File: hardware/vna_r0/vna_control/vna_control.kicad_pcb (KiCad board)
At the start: 2 copper layers, 111 parts, among them J301 CONN_02X10, J302 CONN_02X10, J303 CONN_02X10, J304 CONN_02X23, J305 CONN_01X02, J306 CONN_02X23, J307 BARREL_JACK, J401 CONN_01X02, Q301 DMG2305UX, U201 AD9577, U202 CONN_SMA_2GND, U301 CONN_SMA, U302 CONN_SMA, U303 CONN_SMA, U304 CONN_SMA, U305 CONN_SMA, U401 ADP7158, U402 ADP7158, U403 ADP7158, U404 OKR-T/3-W12-C, U405 TPS2041B, U406 LTC1983, Y201 26 MHz FX532A

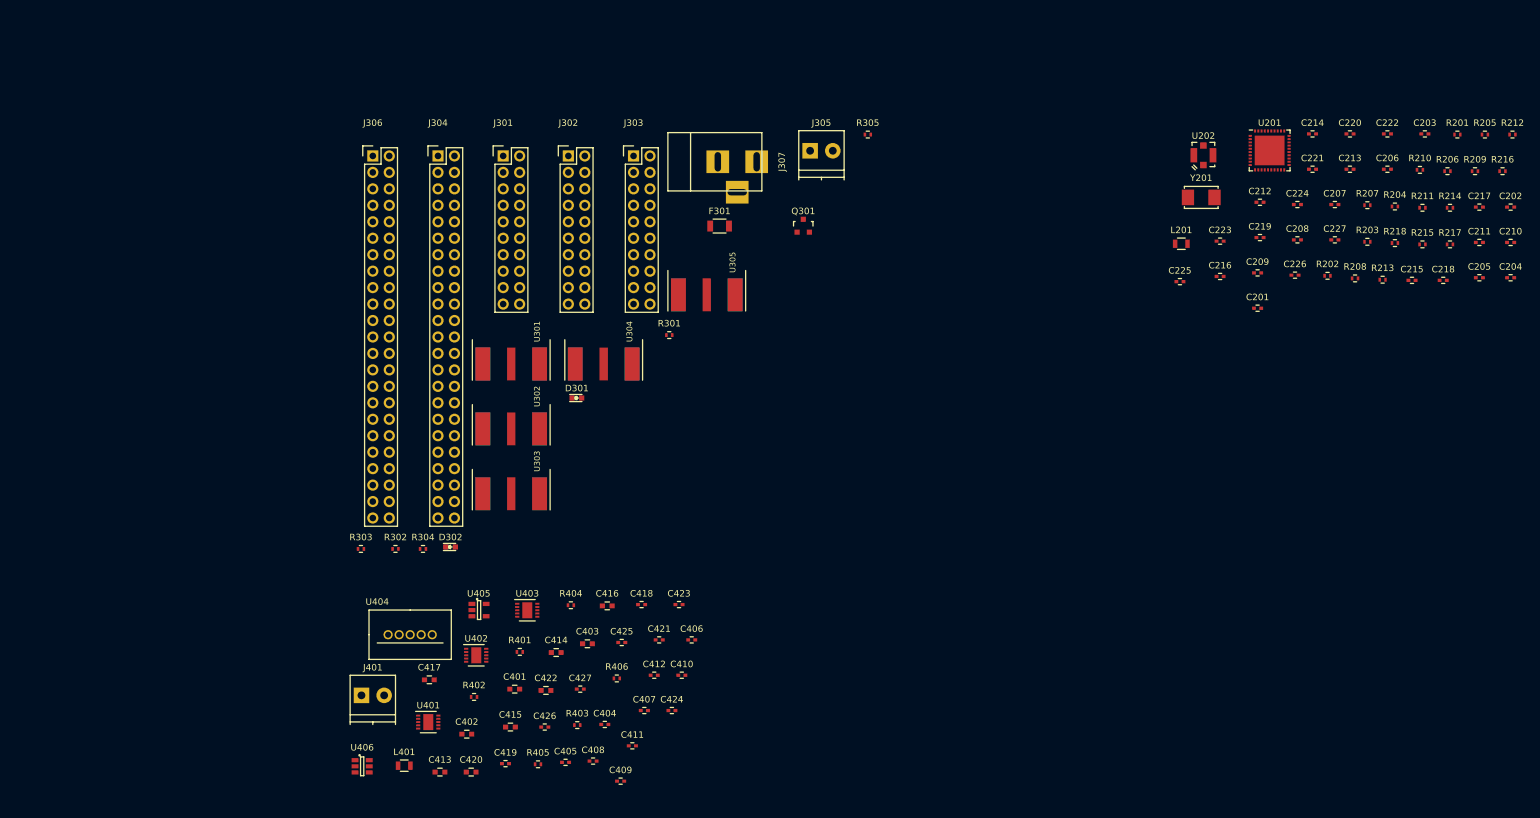
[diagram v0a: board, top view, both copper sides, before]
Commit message: component placement on vna cape..
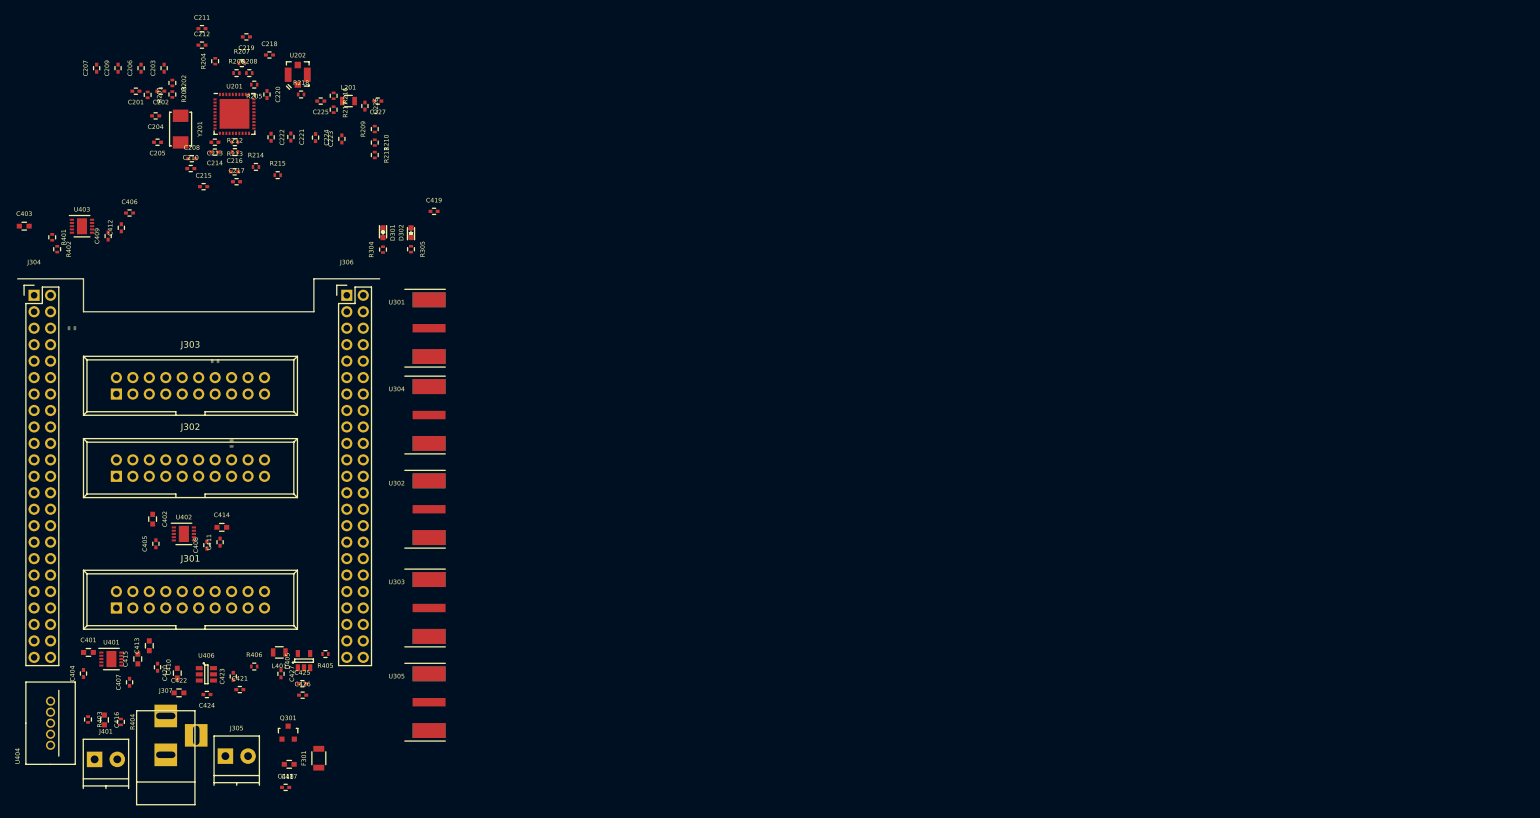
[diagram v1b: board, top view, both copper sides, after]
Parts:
- J301, J302, J303: footprint Pin_Headers:Pin_Header_Straight_2x10 -> Connect:IDC_Header_Straight_20pins
- R301, R302, R303: moved to B.Cu
- moved C204 210.6 mm to (54.3, 40.9), turned to 180 degrees
- moved C202 209.1 mm to (55.1, 37.1), turned to 180 degrees
- moved C205 205.1 mm to (54.6, 45.0), turned to 180 degrees
- moved C210 204.0 mm to (59.7, 49.0)
- moved R201 202.2 mm to (53.1, 37.6), turned to 270 degrees
- moved C211 199.9 mm to (61.5, 27.4)
- moved R212 197.2 mm to (66.5, 46.5)
- moved C203 194.8 mm to (55.6, 33.5), turned to 90 degrees
- moved C206 193.0 mm to (52.1, 33.5), turned to 90 degrees
- moved C207 192.3 mm to (45.2, 33.5), turned to 90 degrees
- moved C217 191.9 mm to (66.8, 51.1)
- moved R205 190.1 mm to (69.5, 36.1), turned to 180 degrees
- moved R206 187.5 mm to (66.8, 34.3)
- moved C215 187.1 mm to (61.7, 51.8)
- moved R203 185.8 mm to (56.9, 37.6), turned to 270 degrees
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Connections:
- D301 pad 1: (no net) -> GND
- D302 pad 2: (no net) -> GND
- R304 pad 1: /connecors/3V3_RF -> +3V3
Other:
- board outline added: 55.9 x 5.1 mm
- copper layers 2 -> 4
- rule pad_to_mask_clearance: 0.2 -> 0.05

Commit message: layout of control cape..
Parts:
- removed C417: CP_Small, Capacitors_SMD:C_0603
- removed C419: 100 nF, Capacitors_SMD:C_0402
- added C428: 100 uF, Capacitors_SMD:c_elec_10x10, F.Cu at (73.2, 123.3)
- R402: moved to B.Cu
- R404: footprint Resistors_SMD:R_0402 -> Resistors_SMD:R_1206
- moved D302 73.6 mm to (43.9, 113.2)
- moved R305 73.6 mm to (43.9, 115.6), turned to 90 degrees
- moved C211 51.4 mm to (64.8, 78.7), turned to 180 degrees
- moved C227 49.8 mm to (80.3, 87.7), turned to 90 degrees
- moved C212 47.6 mm to (64.8, 77.5), turned to 180 degrees
- moved C219 47.2 mm to (68.8, 75.9)
- moved C207 46.9 mm to (59.2, 78.3)
- moved R209 46.8 mm to (77.0, 88.4)
- moved C226 46.7 mm to (79.8, 85.6), turned to 180 degrees
- moved C209 46.3 mm to (60.5, 78.2)
- moved C218 45.8 mm to (68.8, 77.2), turned to 180 degrees
- moved C206 45.7 mm to (61.7, 78.2)
- moved C203 45.3 mm to (63.0, 78.2)
- moved C201 45.0 mm to (52.8, 82.0), turned to 270 degrees
- moved L201 44.8 mm to (80.3, 83.2), turned to 270 degrees
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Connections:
- C427 pad 1: +5V -> Net-(C427-Pad1)
- J401 pad 1: GND -> VPP
- J401 pad 2: VPP -> GND
- L401 pad 1: Net-(L401-Pad1) -> Net-(C427-Pad1)
- U405 pad 5: Net-(L401-Pad1) -> Net-(C427-Pad1)
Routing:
- net +3V3: track 0.00 -> 74.3 mm, vias 0 -> 18
- net GND: track 0.00 -> 66.5 mm, vias 0 -> 80
- net +5V: track 0.00 -> 44.6 mm, vias 0 -> 2
- net VPP: track 0.00 -> 33.3 mm
- net Net-(F301-Pad2): track 0.00 -> 15.9 mm
- net /3V3_PLL_EN: track 0.00 -> 11.7 mm, vias 0 -> 2
- net /clock_gen/OUT1N: track 0.00 -> 11.1 mm
- net Net-(C205-Pad1): track 0.00 -> 10.6 mm
- net Net-(C204-Pad1): track 0.00 -> 10.0 mm
- net Net-(C202-Pad1): track 0.00 -> 9.99 mm
- net /clock_gen/OUT0P: track 0.00 -> 8.78 mm
- net /clock_gen/OUT0N: track 0.00 -> 8.54 mm
- net /clock_gen/OUT3P: track 0.00 -> 8.45 mm
- net /clock_gen/SYNTH_REF_B: track 0.00 -> 7.71 mm
- net Net-(R404-Pad2): track 0.00 -> 7.68 mm
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- added copper zone on F.Cu, net GND
- added copper zone on In1.Cu, net GND
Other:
- board size 55.9 x 5.1 mm -> 73.7 x 76.2 mm
- net class Default: clearance 0.2 -> 0.126
- rule trace_clearance: 0.2 -> 0.126
- board text added: "3V6"
- board text added: "5V IN"
- board text added: "demod"
- board text added: "rf"
- board text added: "vna control cape r1 2017.07"

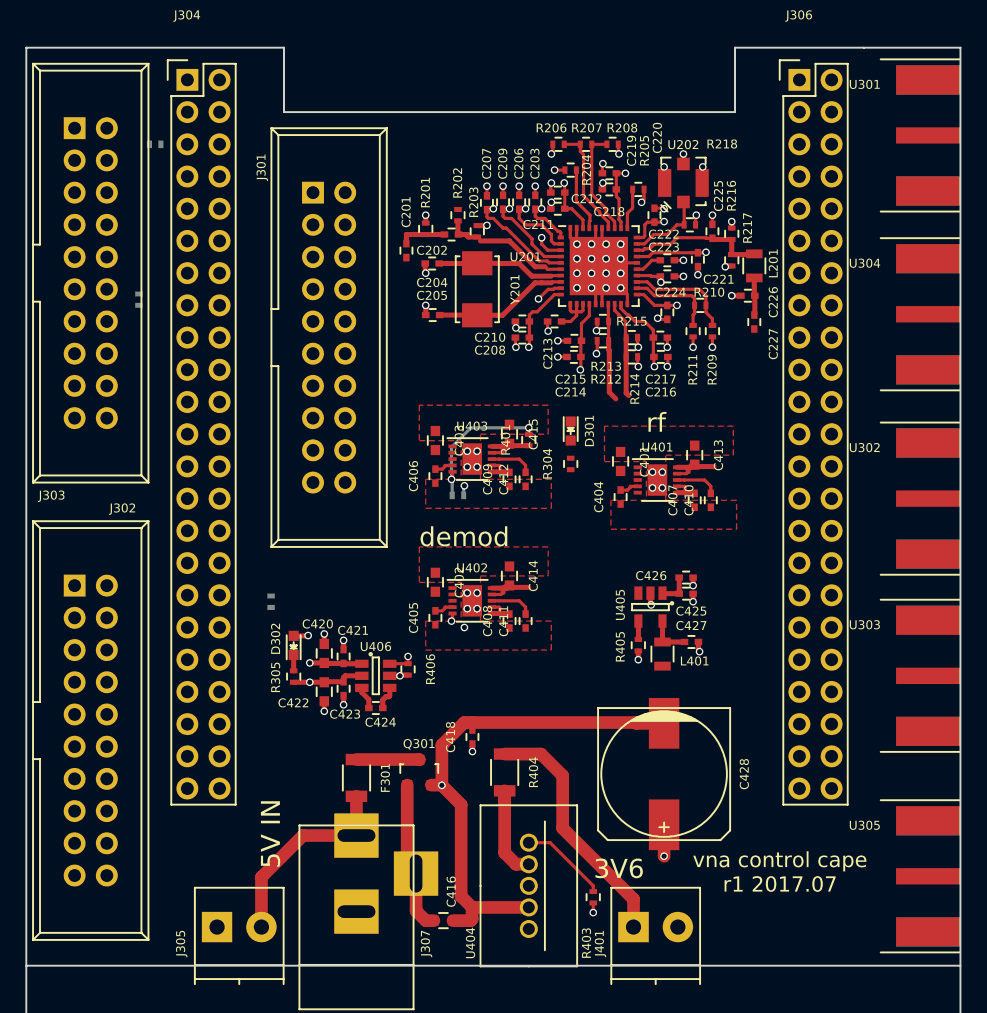
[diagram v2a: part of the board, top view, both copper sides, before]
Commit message: vna control cape layout - all nets connected
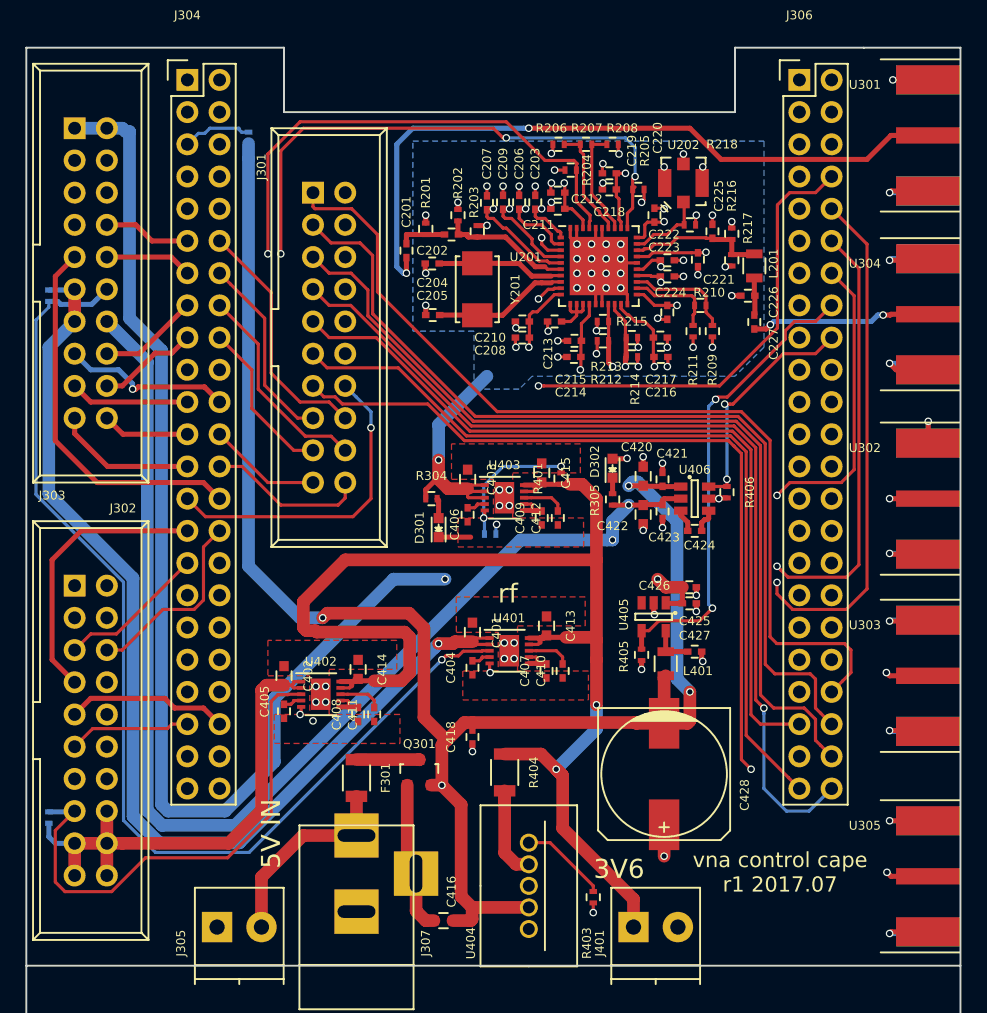
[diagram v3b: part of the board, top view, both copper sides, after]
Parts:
- moved C421 28.8 mm to (73.0, 100.1)
- moved C420 28.8 mm to (71.5, 99.8)
- moved C422 28.8 mm to (71.5, 102.9)
- moved C423 28.8 mm to (73.0, 102.6)
- moved C424 28.8 mm to (75.6, 104.1)
- moved R406 28.8 mm to (78.1, 101.1)
- moved U406 28.8 mm to (75.6, 101.6)
- moved D302 28.8 mm to (69.1, 99.2)
- moved R305 28.8 mm to (69.1, 101.7)
- moved R301 24.4 mm to (24.6, 126.7)
- moved C401 17.8 mm to (58.0, 112.1)
- moved C404 17.8 mm to (58.0, 114.9)
- moved C407 17.8 mm to (63.9, 115.2)
- moved C410 17.8 mm to (65.2, 115.2)
- moved C413 17.8 mm to (63.9, 111.6)
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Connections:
- J304 pad 13: /connecors/DEMOD_LMX_MUXOUT -> /connecors/RF_LMX_CE
- J304 pad 15: (no net) -> /connecors/RF_PORT_SEL
- J304 pad 16: /connecors/AD_PE_B -> /connecors/AD_PE_A
- J304 pad 18: /connecors/AD_PE_A -> /connecors/AD_PE_C
- J304 pad 23: /connecors/RF_SW_1 -> /connecors/RF_SW_2
- J304 pad 25: /connecors/RF_SW_2 -> /connecors/RF_SW_1
- J304 pad 26: /connecors/AD_PE_C -> /connecors/AD_PE_B
- J304 pad 27: /connecors/RF_PORT_SEL -> /connecors/AD_DOUTB
- J304 pad 30: (no net) -> /connecors/DEMOD_LMX_MUXOUT
- J304 pad 41: (no net) -> /connecors/DEMOD_LMX_CE
- J306 pad 10: /3V3_PLL_EN -> /3V3_RF_EN
- J306 pad 11: /connecors/RF_LMX_CE -> (no net)
- J306 pad 12: /3V3_RF_EN -> /3V3_DEMOD_EN
- J306 pad 13: /connecors/DEMOD_LMX_CE -> (no net)
- J306 pad 14: /3V3_DEMOD_EN -> /3V3_PLL_EN
- J306 pad 15: /connecors/MIX_EN -> (no net)
- J306 pad 17: /connecors/MIX_X2 -> (no net)
- J306 pad 26: /connecors/AD_DOUTB -> (no net)
- J306 pad 27: (no net) -> /connecors/MIX_X2
- J306 pad 28: (no net) -> /connecors/MIX_EN
- J306 pad 29: (no net) -> /connecors/IF_REF_EN
- J306 pad 30: (no net) -> /connecors/ADC_CLK_EN
- J306 pad 7: /connecors/IF_REF_EN -> (no net)
- J306 pad 9: /connecors/ADC_CLK_EN -> (no net)
- U302 pad 1: /clock_gen/SYNTH_REF_B -> /clock_gen/SYNTH_REF_A
- U303 pad 1: /clock_gen/SYNTH_REF_A -> /clock_gen/SYNTH_REF_B
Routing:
- net /connecors/AMP_5V: track 2.60 -> 113.5 mm, vias 0 -> 2
- net -5V: track 5.79 -> 95.4 mm, vias 1 -> 2
- net +5V: track 44.6 -> 131.8 mm, vias 2 -> 4
- net /connecors/3V3_RF_SENSE: track 0.00 -> 85.9 mm, vias 0 -> 1
- net /connecors/3V3_RF: track 0.00 -> 84.3 mm, vias 0 -> 1
- net /clock_gen/ADC_CLK: track 2.21 -> 84.8 mm, vias 1 -> 2
- net /3V3_DEMOD_EN: track 0.71 -> 82.1 mm, vias 1 -> 2
- net /connecors/AD_DOUTA_A: track 0.00 -> 74.0 mm, vias 0 -> 1
- net /connecors/AD_DOUTA_D: track 0.00 -> 73.7 mm
- net /connecors/AD_DOUTA_C: track 0.00 -> 71.4 mm
- net /connecors/AD_DOUTA_B: track 0.00 -> 70.9 mm
- net VPP: track 33.3 -> 103.7 mm, vias 0 -> 2
- net /3V3_RF_EN: track 0.00 -> 66.6 mm, vias 0 -> 2
- net /connecors/AD_CLKOUT: track 0.00 -> 65.7 mm
- net /connecors/AD_FS: track 0.00 -> 65.4 mm, vias 0 -> 1
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- added copper zone on B.Cu, net +3V3
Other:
- board text removed: "demod"

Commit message: finished vna control cape
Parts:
- added G***: LOGO, vna_footprints:snail, B.Cu at (83.3, 134.1)
- added REF**: VIA_OSH4LAYER_MIN, vna_footprints:VIA_OSH4LAYER_MIN, F.Cu at (56.5, 99.1)
- added REF**: VIA_OSH4LAYER_MIN, vna_footprints:VIA_OSH4LAYER_MIN, F.Cu at (52.7, 99.1)
- added REF**: VIA_OSH4LAYER_MIN, vna_footprints:VIA_OSH4LAYER_MIN, F.Cu at (52.7, 101.0)
- added REF**: VIA_OSH4LAYER_MIN, vna_footprints:VIA_OSH4LAYER_MIN, F.Cu at (52.7, 102.9)
- added REF**: VIA_OSH4LAYER_MIN, vna_footprints:VIA_OSH4LAYER_MIN, F.Cu at (52.7, 104.8)
- added REF**: VIA_OSH4LAYER_MIN, vna_footprints:VIA_OSH4LAYER_MIN, F.Cu at (56.5, 102.2)
- added REF**: VIA_OSH4LAYER_MIN, vna_footprints:VIA_OSH4LAYER_MIN, F.Cu at (56.5, 103.5)
- added REF**: VIA_OSH4LAYER_MIN, vna_footprints:VIA_OSH4LAYER_MIN, F.Cu at (61.0, 104.1)
- added REF**: VIA_OSH4LAYER_MIN, vna_footprints:VIA_OSH4LAYER_MIN, F.Cu at (62.2, 103.5)
- added REF**: VIA_OSH4LAYER_MIN, vna_footprints:VIA_OSH4LAYER_MIN, F.Cu at (66.0, 103.5)
- added REF**: VIA_OSH4LAYER_MIN, vna_footprints:VIA_OSH4LAYER_MIN, F.Cu at (66.0, 116.2)
- added REF**: VIA_OSH4LAYER_MIN, vna_footprints:VIA_OSH4LAYER_MIN, F.Cu at (58.4, 99.1)
- added REF**: VIA_OSH4LAYER_MIN, vna_footprints:VIA_OSH4LAYER_MIN, F.Cu at (66.0, 117.5)
- added REF**: VIA_OSH4LAYER_MIN, vna_footprints:VIA_OSH4LAYER_MIN, F.Cu at (65.4, 116.8)
- added REF**: VIA_OSH4LAYER_MIN, vna_footprints:VIA_OSH4LAYER_MIN, F.Cu at (64.1, 116.8)
- added REF**: VIA_OSH4LAYER_MIN, vna_footprints:VIA_OSH4LAYER_MIN, F.Cu at (63.5, 117.5)
- added REF**: VIA_OSH4LAYER_MIN, vna_footprints:VIA_OSH4LAYER_MIN, F.Cu at (61.6, 116.2)
- added REF**: VIA_OSH4LAYER_MIN, vna_footprints:VIA_OSH4LAYER_MIN, F.Cu at (61.6, 117.5)
- added REF**: VIA_OSH4LAYER_MIN, vna_footprints:VIA_OSH4LAYER_MIN, F.Cu at (59.7, 117.5)
- added REF**: VIA_OSH4LAYER_MIN, vna_footprints:VIA_OSH4LAYER_MIN, F.Cu at (59.7, 116.2)
- added REF**: VIA_OSH4LAYER_MIN, vna_footprints:VIA_OSH4LAYER_MIN, F.Cu at (57.8, 116.2)
- added REF**: VIA_OSH4LAYER_MIN, vna_footprints:VIA_OSH4LAYER_MIN, F.Cu at (57.8, 117.5)
- added REF**: VIA_OSH4LAYER_MIN, vna_footprints:VIA_OSH4LAYER_MIN, F.Cu at (66.0, 99.1)
- added REF**: VIA_OSH4LAYER_MIN, vna_footprints:VIA_OSH4LAYER_MIN, F.Cu at (55.9, 117.5)
- added REF**: VIA_OSH4LAYER_MIN, vna_footprints:VIA_OSH4LAYER_MIN, F.Cu at (55.9, 116.2)
- added REF**: VIA_OSH4LAYER_MIN, vna_footprints:VIA_OSH4LAYER_MIN, F.Cu at (66.7, 109.2)
- added REF**: VIA_OSH4LAYER_MIN, vna_footprints:VIA_OSH4LAYER_MIN, F.Cu at (66.7, 110.5)
- added REF**: VIA_OSH4LAYER_MIN, vna_footprints:VIA_OSH4LAYER_MIN, F.Cu at (65.4, 110.5)
- added REF**: VIA_OSH4LAYER_MIN, vna_footprints:VIA_OSH4LAYER_MIN, F.Cu at (65.4, 109.2)
- added REF**: VIA_OSH4LAYER_MIN, vna_footprints:VIA_OSH4LAYER_MIN, F.Cu at (64.1, 109.2)
- added REF**: VIA_OSH4LAYER_MIN, vna_footprints:VIA_OSH4LAYER_MIN, F.Cu at (62.9, 109.2)
- added REF**: VIA_OSH4LAYER_MIN, vna_footprints:VIA_OSH4LAYER_MIN, F.Cu at (62.9, 110.5)
- added REF**: VIA_OSH4LAYER_MIN, vna_footprints:VIA_OSH4LAYER_MIN, F.Cu at (61.6, 109.2)
- added REF**: VIA_OSH4LAYER_MIN, vna_footprints:VIA_OSH4LAYER_MIN, F.Cu at (66.0, 97.8)
- added REF**: VIA_OSH4LAYER_MIN, vna_footprints:VIA_OSH4LAYER_MIN, F.Cu at (61.6, 110.5)
- added REF**: VIA_OSH4LAYER_MIN, vna_footprints:VIA_OSH4LAYER_MIN, F.Cu at (60.3, 109.2)
- added REF**: VIA_OSH4LAYER_MIN, vna_footprints:VIA_OSH4LAYER_MIN, F.Cu at (60.3, 110.5)
- added REF**: VIA_OSH4LAYER_MIN, vna_footprints:VIA_OSH4LAYER_MIN, F.Cu at (59.1, 109.2)
- added REF**: VIA_OSH4LAYER_MIN, vna_footprints:VIA_OSH4LAYER_MIN, F.Cu at (59.1, 110.5)
- added REF**: VIA_OSH4LAYER_MIN, vna_footprints:VIA_OSH4LAYER_MIN, F.Cu at (57.8, 110.5)
- added REF**: VIA_OSH4LAYER_MIN, vna_footprints:VIA_OSH4LAYER_MIN, F.Cu at (56.5, 111.8)
- added REF**: VIA_OSH4LAYER_MIN, vna_footprints:VIA_OSH4LAYER_MIN, F.Cu at (55.9, 109.2)
- added REF**: VIA_OSH4LAYER_MIN, vna_footprints:VIA_OSH4LAYER_MIN, F.Cu at (52.1, 123.8)
- added REF**: VIA_OSH4LAYER_MIN, vna_footprints:VIA_OSH4LAYER_MIN, F.Cu at (47.0, 123.8)
- added REF**: VIA_OSH4LAYER_MIN, vna_footprints:VIA_OSH4LAYER_MIN, F.Cu at (64.1, 97.8)
- added REF**: VIA_OSH4LAYER_MIN, vna_footprints:VIA_OSH4LAYER_MIN, F.Cu at (51.4, 119.4)
- added REF**: VIA_OSH4LAYER_MIN, vna_footprints:VIA_OSH4LAYER_MIN, F.Cu at (51.4, 120.7)
- added REF**: VIA_OSH4LAYER_MIN, vna_footprints:VIA_OSH4LAYER_MIN, F.Cu at (50.2, 120.7)
- added REF**: VIA_OSH4LAYER_MIN, vna_footprints:VIA_OSH4LAYER_MIN, F.Cu at (43.8, 121.3)
- added REF**: VIA_OSH4LAYER_MIN, vna_footprints:VIA_OSH4LAYER_MIN, F.Cu at (45.1, 120.0)
- added REF**: VIA_OSH4LAYER_MIN, vna_footprints:VIA_OSH4LAYER_MIN, F.Cu at (43.8, 120.0)
- added REF**: VIA_OSH4LAYER_MIN, vna_footprints:VIA_OSH4LAYER_MIN, F.Cu at (50.2, 114.9)
- added REF**: VIA_OSH4LAYER_MIN, vna_footprints:VIA_OSH4LAYER_MIN, F.Cu at (50.2, 113.7)
- added REF**: VIA_OSH4LAYER_MIN, vna_footprints:VIA_OSH4LAYER_MIN, F.Cu at (48.9, 113.7)
- added REF**: VIA_OSH4LAYER_MIN, vna_footprints:VIA_OSH4LAYER_MIN, F.Cu at (47.6, 113.7)
- added REF**: VIA_OSH4LAYER_MIN, vna_footprints:VIA_OSH4LAYER_MIN, F.Cu at (62.2, 97.8)
- added REF**: VIA_OSH4LAYER_MIN, vna_footprints:VIA_OSH4LAYER_MIN, F.Cu at (47.6, 114.9)
- added REF**: VIA_OSH4LAYER_MIN, vna_footprints:VIA_OSH4LAYER_MIN, F.Cu at (43.2, 113.7)
- added REF**: VIA_OSH4LAYER_MIN, vna_footprints:VIA_OSH4LAYER_MIN, F.Cu at (41.9, 113.7)
- added REF**: VIA_OSH4LAYER_MIN, vna_footprints:VIA_OSH4LAYER_MIN, F.Cu at (41.9, 114.9)
- added REF**: VIA_OSH4LAYER_MIN, vna_footprints:VIA_OSH4LAYER_MIN, F.Cu at (40.6, 114.9)
- added REF**: VIA_OSH4LAYER_MIN, vna_footprints:VIA_OSH4LAYER_MIN, F.Cu at (60.3, 97.8)
- added REF**: VIA_OSH4LAYER_MIN, vna_footprints:VIA_OSH4LAYER_MIN, F.Cu at (58.4, 97.8)
- added REF**: VIA_OSH4LAYER_MIN, vna_footprints:VIA_OSH4LAYER_MIN, F.Cu at (56.5, 97.8)
- Y201: value 26 MHz FX532A -> 26 MHz 7M-26.000MEEQ-T; footprint Crystals:ABM3 -> vna_footprints:crystal_FA238-TSX3225
- moved C205 3.78 mm to (58.7, 87.4)
- moved C204 1.89 mm to (56.7, 83.6)
- moved Y201 1.07 mm to (59.4, 84.7)
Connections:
- Y201 pad 2: Net-(C205-Pad1) -> GND
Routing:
- net Net-(C205-Pad1): track 10.6 -> 7.76 mm
- net GND: track 127.4 -> 129.5 mm, vias 90 -> 92
- net Net-(C204-Pad1): track 10.0 -> 9.35 mm
- added copper zone on B.Cu, net GND
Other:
- board size 73.7 x 76.2 mm -> 73.7 x 72.4 mm
- board text added: "ADC CLK"
- board text added: "BBONE EXT 5V JMP"
- board text added: "DEMOD J401"
- board text added: "DEMOD J402"
- board text added: "DEMOD VREG SENSE BYPASS JMP"
- board text added: "GND"
- board text added: "IF REF"
- board text added: "PLL REF IN"
- board text added: "RF J401"
- board text added: "RF VREG SENSE BYPASS JMP"
- board text added: "SYNTH REF A"
- board text added: "SYNTH REF B"
- board text removed: "rf"
